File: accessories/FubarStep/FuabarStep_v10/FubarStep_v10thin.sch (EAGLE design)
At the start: 57 parts, among them IC1 OKI-78SR-5/1.5-W36H-C, IC2 SN754410NE, IC3 SN754410NE, X1 DC21MMX

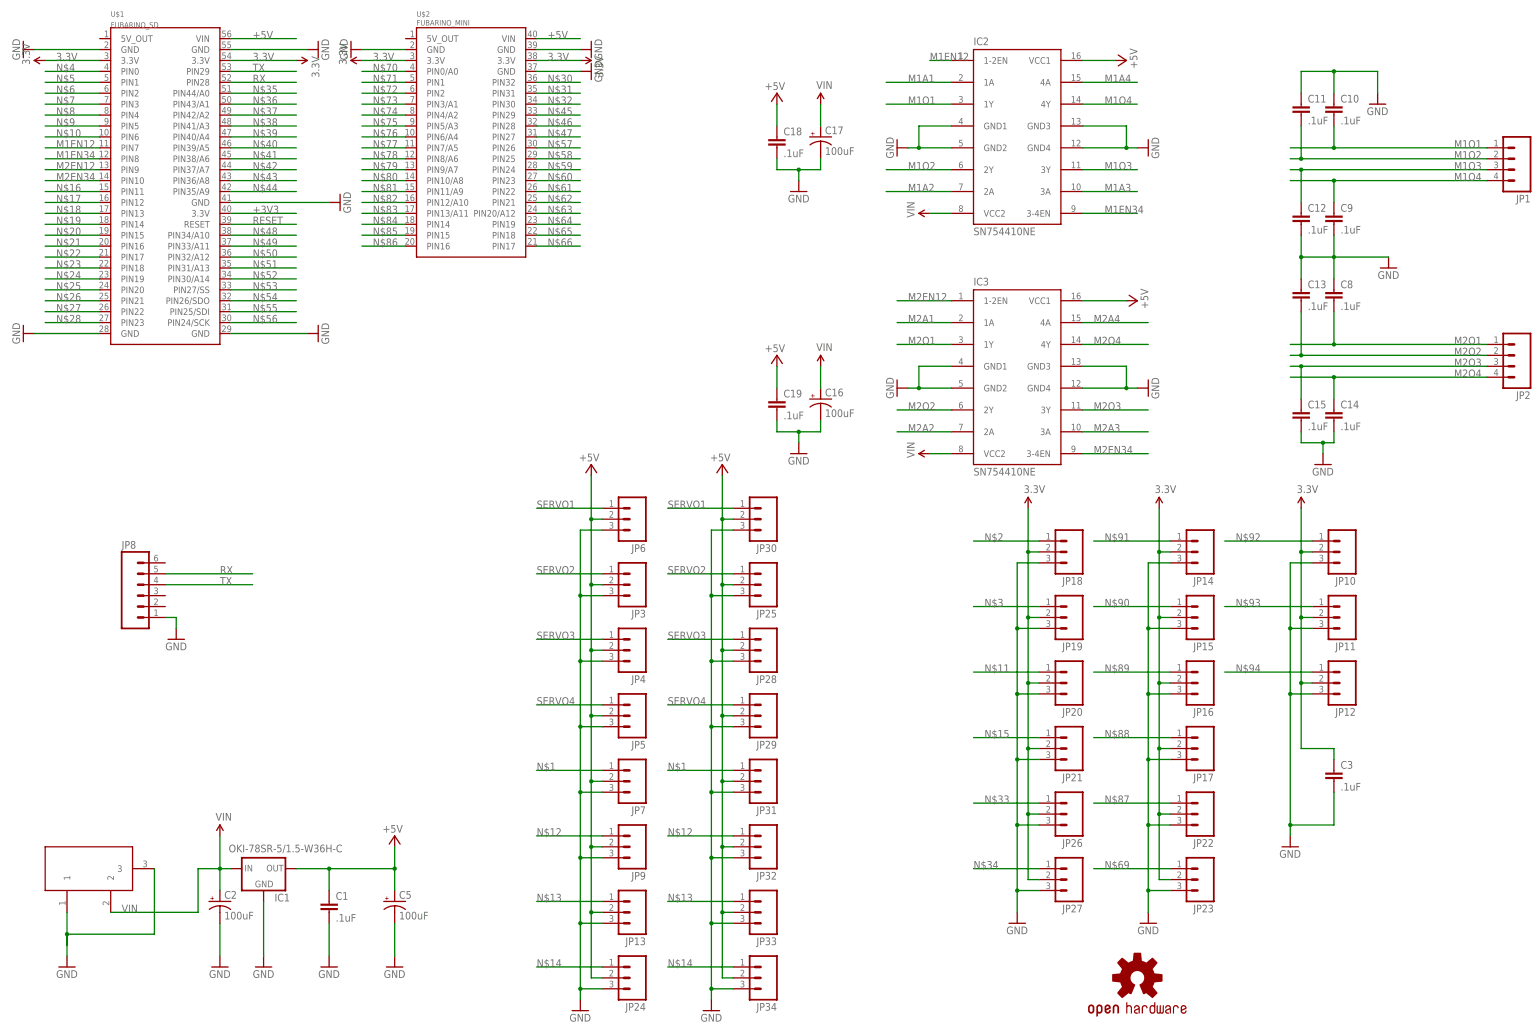
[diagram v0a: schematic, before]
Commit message: Started routing. And assigned all the pins except for Mini to SD.
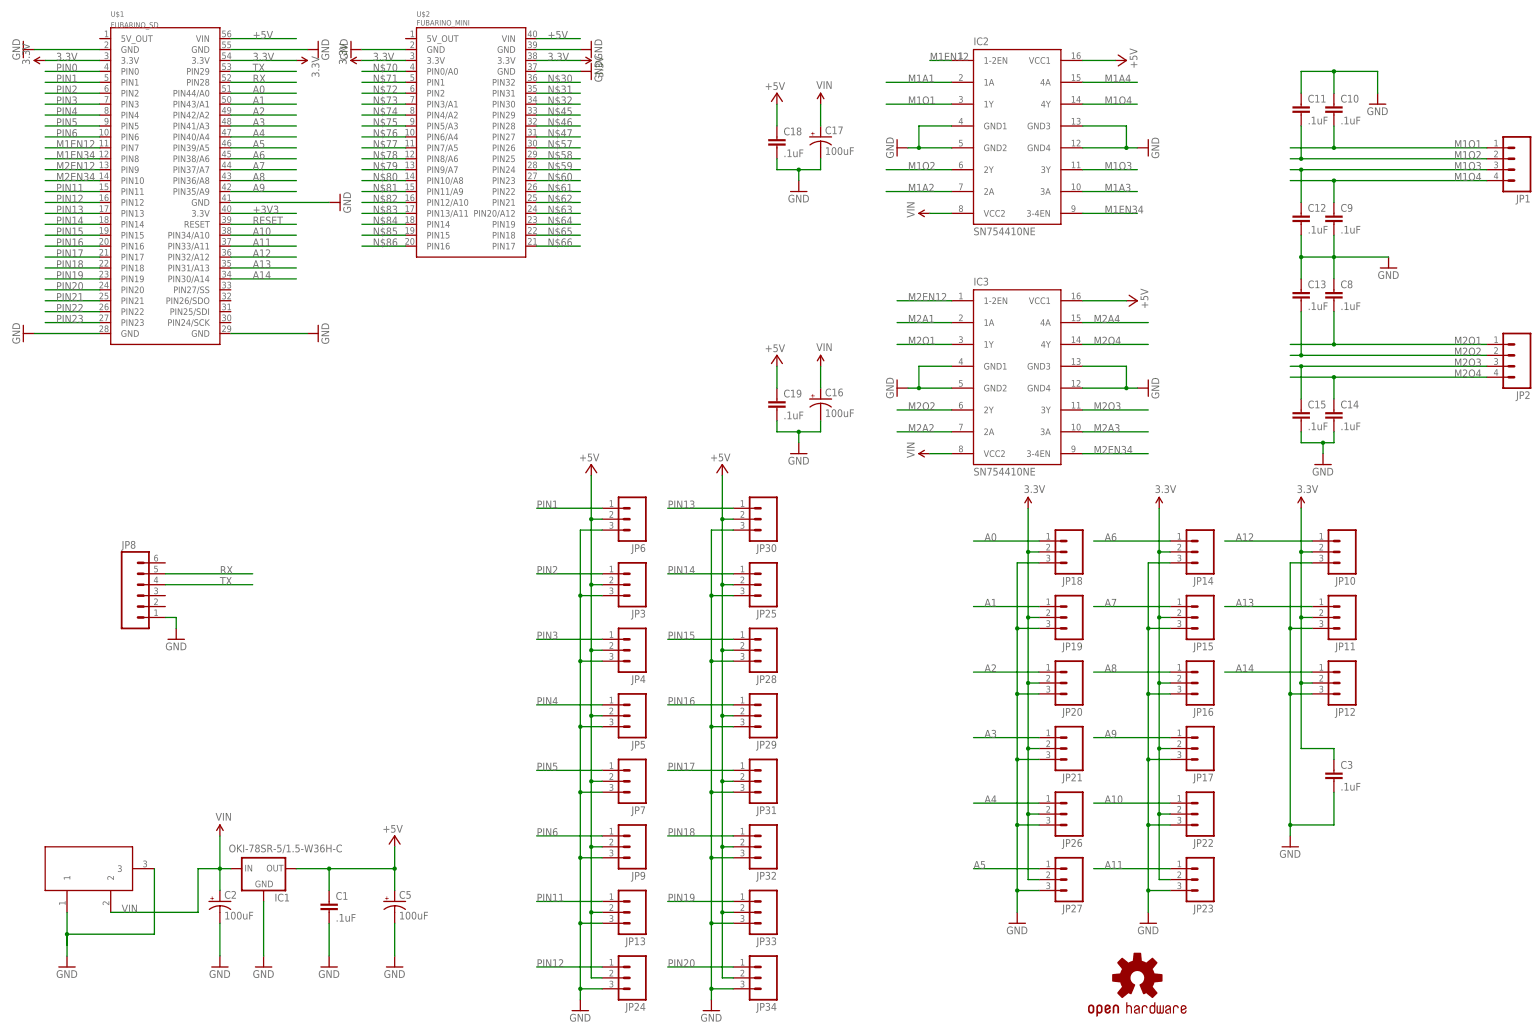
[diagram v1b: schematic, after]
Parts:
- JP10, JP11, JP12, JP13, JP14, JP15, JP16, JP17, JP18, JP19, JP20, JP21, JP22, JP23, JP24, JP25, JP26, JP27, JP28, JP29, JP3, JP30, JP31, JP32, JP33, JP34, JP4, JP5, JP6, JP7, JP9: device SparkFun-Connectors:M03LOCK -> SparkFun-Connectors:M03PTH
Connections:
- net N$26 renamed PIN21
- net N$27 renamed PIN22
- net N$28 renamed PIN23
- net N$4 renamed PIN0
- removed net N$1: JP31.1, JP7.1
- removed net N$10: U$1.PIN6
- removed net N$11: JP20.1
- removed net N$12: JP32.1, JP9.1
- removed net N$13: JP13.1, JP33.1
- removed net N$14: JP24.1, JP34.1
- removed net N$15: JP21.1
- removed net N$16: U$1.PIN11
- removed net N$17: U$1.PIN12
- removed net N$18: U$1.PIN13
- removed net N$19: U$1.PIN14
- removed net N$2: JP18.1
- removed net N$20: U$1.PIN15
- removed net N$21: U$1.PIN16
- removed net N$22: U$1.PIN17
- removed net N$23: U$1.PIN18
- removed net N$24: U$1.PIN19
- removed net N$25: U$1.PIN20
- removed net N$3: JP19.1
- removed net N$33: JP26.1
- removed net N$34: JP27.1
- removed net N$35: U$1.PIN44/A0
- removed net N$36: U$1.PIN43/A1
- removed net N$37: U$1.PIN42/A2
- removed net N$38: U$1.PIN41/A3
- removed net N$39: U$1.PIN40/A4
- removed net N$40: U$1.PIN39/A5
- removed net N$41: U$1.PIN38/A6
- removed net N$42: U$1.PIN37/A7
- removed net N$43: U$1.PIN36/A8
- removed net N$44: U$1.PIN35/A9
- removed net N$48: U$1.PIN34/A10
- removed net N$49: U$1.PIN33/A11
- removed net N$5: U$1.PIN1
- removed net N$50: U$1.PIN32/A12
- removed net N$51: U$1.PIN31/A13
- removed net N$52: U$1.PIN30/A14
- removed net N$53: U$1.PIN27/SS
- removed net N$54: U$1.PIN26/SDO
- removed net N$55: U$1.PIN25/SDI
- removed net N$56: U$1.PIN24/SCK
- removed net N$6: U$1.PIN2
- removed net N$69: JP23.1
- removed net N$7: U$1.PIN3
- removed net N$8: U$1.PIN4
- removed net N$87: JP22.1
- removed net N$88: JP17.1
- removed net N$89: JP16.1
- removed net N$9: U$1.PIN5
- removed net N$90: JP15.1
- removed net N$91: JP14.1
- removed net N$92: JP10.1
- removed net N$93: JP11.1
- removed net N$94: JP12.1
- removed net SERVO1: JP30.1, JP6.1
- removed net SERVO2: JP25.1, JP3.1
- removed net SERVO3: JP28.1, JP4.1
- removed net SERVO4: JP29.1, JP5.1
- new net A0: JP18.1, U$1.PIN44/A0
- new net A1: JP19.1, U$1.PIN43/A1
- new net A10: JP22.1, U$1.PIN34/A10
- new net A11: JP23.1, U$1.PIN33/A11
- new net A12: JP10.1, U$1.PIN32/A12
- new net A13: JP11.1, U$1.PIN31/A13
- new net A14: JP12.1, U$1.PIN30/A14
- new net A2: JP20.1, U$1.PIN42/A2
- new net A3: JP21.1, U$1.PIN41/A3
- new net A4: JP26.1, U$1.PIN40/A4
- new net A5: JP27.1, U$1.PIN39/A5
- new net A6: JP14.1, U$1.PIN38/A6
- new net A7: JP15.1, U$1.PIN37/A7
- new net A8: JP16.1, U$1.PIN36/A8
- new net A9: JP17.1, U$1.PIN35/A9
- new net PIN1: JP6.1, U$1.PIN1
- new net PIN11: JP13.1, U$1.PIN11
- new net PIN12: JP24.1, U$1.PIN12
- new net PIN13: JP30.1, U$1.PIN13
- new net PIN14: JP25.1, U$1.PIN14
- new net PIN15: JP28.1, U$1.PIN15
- new net PIN16: JP29.1, U$1.PIN16
- new net PIN17: JP31.1, U$1.PIN17
- new net PIN18: JP32.1, U$1.PIN18
- new net PIN19: JP33.1, U$1.PIN19
- new net PIN2: JP3.1, U$1.PIN2
- new net PIN20: JP34.1, U$1.PIN20
- new net PIN3: JP4.1, U$1.PIN3
- new net PIN4: JP5.1, U$1.PIN4
- new net PIN5: JP7.1, U$1.PIN5
- new net PIN6: JP9.1, U$1.PIN6

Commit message: More routing.
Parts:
- removed JP3, JP4, JP5, JP6: (no value), SparkFun-Connectors:M03PTH
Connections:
- removed net PIN0: U$1.PIN0
- removed net PIN1: JP6.1, U$1.PIN1
- removed net PIN11: JP13.1, U$1.PIN11
- removed net PIN2: JP3.1, U$1.PIN2
- removed net PIN3: JP4.1, U$1.PIN3
- removed net PIN4: JP5.1, U$1.PIN4
- removed net PIN5: JP7.1, U$1.PIN5
- removed net PIN6: JP9.1, U$1.PIN6
- net +5V: no longer JP3.2, JP4.2, JP5.2, JP6.2
- net GND: no longer JP3.3, JP4.3, JP5.3, JP6.3
- net M1A1: now also U$1.PIN0
- net M1A2: now also U$1.PIN1
- net M1A3: now also U$1.PIN2
- net M1A4: now also U$1.PIN3
- net M2A1: now also U$1.PIN6
- net M2A2: now also U$1.PIN11, U$1.PIN5
- net M2A3: now also U$1.PIN4
- net PIN12: now also JP7.1; no longer JP24.1
- net PIN13: now also JP9.1; no longer JP30.1
- net PIN14: now also JP13.1; no longer JP25.1
- net PIN15: now also JP24.1; no longer JP28.1
- net PIN16: now also JP30.1; no longer JP29.1
- net PIN17: now also JP25.1; no longer JP31.1
- net PIN18: now also JP28.1; no longer JP32.1
- net PIN19: now also JP29.1; no longer JP33.1
- net PIN20: now also JP31.1; no longer JP34.1
- net PIN21: now also JP32.1
- net PIN22: now also JP33.1
- net PIN23: now also JP34.1

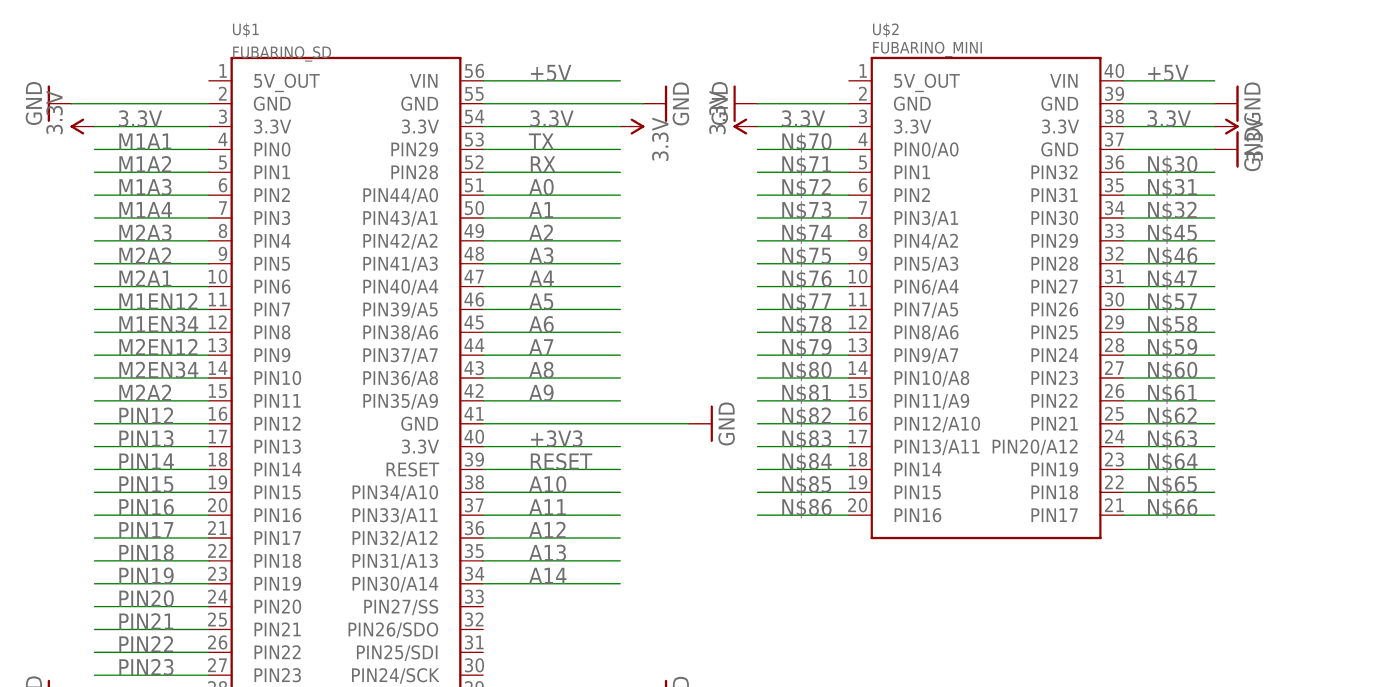
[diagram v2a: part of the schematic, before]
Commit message: Routing is done, but Mini connections not yet made. Top silk is almost done.
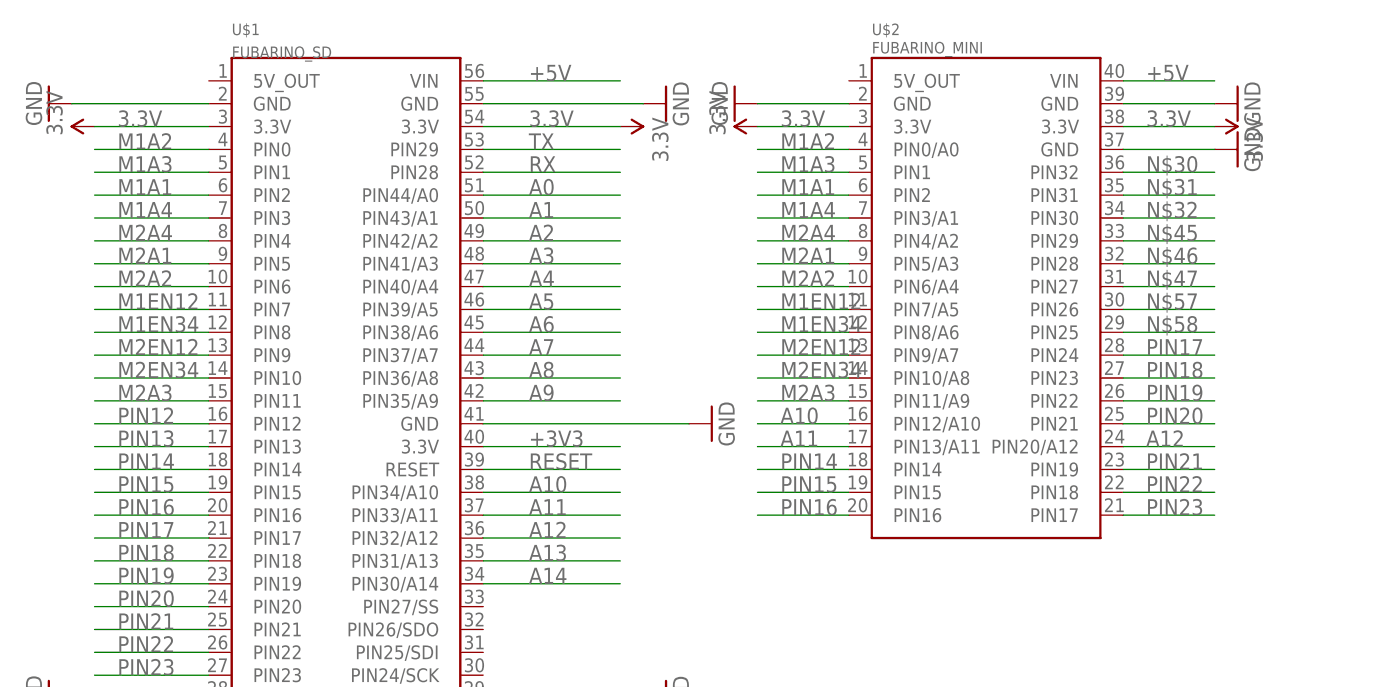
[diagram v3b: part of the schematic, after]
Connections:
- removed net N$59: U$2.PIN24
- removed net N$60: U$2.PIN23
- removed net N$61: U$2.PIN22
- removed net N$62: U$2.PIN21
- removed net N$63: U$2.PIN20/A12
- removed net N$64: U$2.PIN19
- removed net N$65: U$2.PIN18
- removed net N$66: U$2.PIN17
- removed net N$70: U$2.PIN0/A0
- removed net N$71: U$2.PIN1
- removed net N$72: U$2.PIN2
- removed net N$73: U$2.PIN3/A1
- removed net N$74: U$2.PIN4/A2
- removed net N$75: U$2.PIN5/A3
- removed net N$76: U$2.PIN6/A4
- removed net N$77: U$2.PIN7/A5
- removed net N$78: U$2.PIN8/A6
- removed net N$79: U$2.PIN9/A7
- removed net N$80: U$2.PIN10/A8
- removed net N$81: U$2.PIN11/A9
- removed net N$82: U$2.PIN12/A10
- removed net N$83: U$2.PIN13/A11
- removed net N$84: U$2.PIN14
- removed net N$85: U$2.PIN15
- removed net N$86: U$2.PIN16
- net A10: now also U$2.PIN12/A10
- net A11: now also U$2.PIN13/A11
- net A12: now also U$2.PIN20/A12
- net M1A1: now also U$1.PIN2, U$2.PIN2; no longer U$1.PIN0
- net M1A2: now also U$1.PIN0, U$2.PIN0/A0; no longer U$1.PIN1
- net M1A3: now also U$1.PIN1, U$2.PIN1; no longer U$1.PIN2
- net M1A4: now also U$2.PIN3/A1
- net M1EN12: now also U$2.PIN7/A5
- net M1EN34: now also U$2.PIN8/A6
- net M2A1: now also U$1.PIN5, U$2.PIN5/A3; no longer U$1.PIN6
- net M2A2: now also U$1.PIN6, U$2.PIN6/A4; no longer U$1.PIN11, U$1.PIN5
- net M2A3: now also U$1.PIN11, U$2.PIN11/A9; no longer U$1.PIN4
- net M2A4: now also U$1.PIN4, U$2.PIN4/A2
- net M2EN12: now also U$2.PIN9/A7
- net M2EN34: now also U$2.PIN10/A8
- net PIN14: now also U$2.PIN14
- net PIN15: now also U$2.PIN15
- net PIN16: now also U$2.PIN16
- net PIN17: now also U$2.PIN24
- net PIN18: now also U$2.PIN23
- net PIN19: now also U$2.PIN22
- net PIN20: now also U$2.PIN21
- net PIN21: now also U$2.PIN19
- net PIN22: now also U$2.PIN18
- net PIN23: now also U$2.PIN17
